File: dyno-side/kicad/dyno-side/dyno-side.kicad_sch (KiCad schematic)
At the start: 18 parts, among them J1 01x02, J2 01x02, J3 01x02, U1 AP2205-50W5-7, U2 TLV9001IDCK, U3 AM26LS32ACN

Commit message: schematics finished -> Waiting for Altium membership to be progressed.
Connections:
- net +5V: now also U3.15 (4B), U3.7 (2B), U3.9 (3B)
- net GND: now also U3.10 (3A), U3.14 (4A), U3.6 (2A)
- no-connect marks 10 -> 4
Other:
- moved on the sheet: C2
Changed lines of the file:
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@@
 	)
 	(junction
+		(at 104.14 50.8)
+		(diameter 0)
+		(color 0 0 0 0)
+	)
+	(junction
+		(at 184.15 38.1)
+		(diameter 0)
+		(color 0 0 0 0)
+	)
+	(junction
 		(at 34.29 43.18)
 		(diameter 0)
@@
 	)
 	(junction
+		(at 107.95 53.34)
+		(diameter 0)
+		(color 0 0 0 0)
+	)
+	(junction
+		(at 104.14 60.96)
+		(diameter 0)
+		(color 0 0 0 0)
+	)
+	(junction
+		(at 104.14 55.88)
+		(diameter 0)
+		(color 0 0 0 0)
+	)
+	(junction
 		(at 173.99 38.1)
 		(diameter 0)
@@
 	)
 	(junction
-		(at 185.42 38.1)
+		(at 107.95 48.26)
+		(diameter 0)
+		(color 0 0 0 0)
+	)
+	(junction
+		(at 107.95 58.42)
 		(diameter 0)
 		(color 0 0 0 0)
@@
 	)
 	(no_connect
-		(at 111.76 50.8)
-	)
-	(no_connect
-		(at 111.76 55.88)
-	)
-	(no_connect
 		(at 147.32 40.64)
 	)
 	(no_connect
-		(at 111.76 43.18)
-	)
-	(no_connect
-		(at 111.76 48.26)
-	)
-	(no_connect
-		(at 111.76 45.72)
-	)
-	(no_connect
 		(at 147.32 43.18)
 	)
@@
 		(at 264.16 43.18)
 	)
-	(no_connect
-		(at 111.76 53.34)
-	)
 	(wire
 		(pts
@@
 	(wire
 		(pts
-			(xy 185.42 38.1) (xy 204.47 38.1)
-		)
-		(stroke
-			(width 0)
-			(type default)
-		)
-	)
-	(wire
-		(pts
 			(xy 60.96 34.29) (xy 63.5 34.29)
 		)
@@
 	(wire
 		(pts
-			(xy 96.52 60.96) (xy 111.76 60.96)
+			(xy 96.52 60.96) (xy 104.14 60.96)
 		)
 		(stroke
@@
 	(wire
 		(pts
+			(xy 107.95 43.18) (xy 107.95 48.26)
+		)
+		(stroke
+			(width 0)
+			(type default)
+		)
+	)
+	(wire
+		(pts
 			(xy 30.48 45.72) (xy 29.21 45.72)
 		)
@@
 	(wire
 		(pts
+			(xy 111.76 43.18) (xy 107.95 43.18)
+		)
+		(stroke
+			(width 0)
+			(type default)
+		)
+	)
+	(wire
+		(pts
+			(xy 107.95 48.26) (xy 107.95 53.34)
+		)
+		(stroke
+			(width 0)
+			(type default)
+		)
+	)
+	(wire
+		(pts
+			(xy 104.14 60.96) (xy 111.76 60.96)
+		)
+		(stroke
+			(width 0)
+			(type default)
+		)
+	)
+	(wire
+		(pts
 			(xy 39.37 27.94) (xy 55.88 27.94)
 		)
@@
 		)
 	)
+	(wire
+		(pts
+			(xy 107.95 53.34) (xy 107.95 58.42)
+		)
+		(stroke
+			(width 0)
+			(type default)
+		)
+	)
 	(polyline
 		(pts
@@
 	(wire
 		(pts
+			(xy 104.14 50.8) (xy 104.14 55.88)
+		)
+		(stroke
+			(width 0)
+			(type default)
+		)
+	)
+	(wire
+		(pts
+			(xy 111.76 48.26) (xy 107.95 48.26)
+		)
+		(stroke
+			(width 0)
+			(type default)
+		)
+	)
+	(wire
+		(pts
 			(xy 83.82 26.67) (xy 83.82 34.29)
 		)
@@
 	(wire
 		(pts
-			(xy 185.42 54.61) (xy 185.42 49.53)
+			(xy 184.15 49.53) (xy 184.15 54.61)
 		)
 		(stroke
@@
 	(wire
 		(pts
-			(xy 182.88 38.1) (xy 185.42 38.1)
+			(xy 104.14 45.72) (xy 104.14 50.8)
+		)
+		(stroke
+			(width 0)
+			(type default)
+		)
+	)
+	(wire
+		(pts
+			(xy 182.88 38.1) (xy 184.15 38.1)
+		)
+		(stroke
+			(width 0)
+			(type default)
+		)
+	)
+	(wire
+		(pts
+			(xy 111.76 50.8) (xy 104.14 50.8)
 		)
 		(stroke
@@
 	(wire
 		(pts
-			(xy 185.42 38.1) (xy 185.42 44.45)
+			(xy 184.15 38.1) (xy 184.15 44.45)
 		)
 		(stroke
@@
 	(wire
 		(pts
+			(xy 111.76 55.88) (xy 104.14 55.88)
+		)
+		(stroke
+			(width 0)
+			(type default)
+		)
+	)
+	(wire
+		(pts
 			(xy 209.55 48.26) (xy 209.55 54.61)
 		)
@@
 	(wire
 		(pts
+			(xy 111.76 53.34) (xy 107.95 53.34)
+		)
+		(stroke
+			(width 0)
+			(type default)
+		)
+	)
+	(wire
+		(pts
 			(xy 55.88 34.29) (xy 55.88 38.1)
 		)
@@
 		)
 	)
+	(wire
+		(pts
+			(xy 184.15 38.1) (xy 204.47 38.1)
+		)
+		(stroke
+			(width 0)
+			(type default)
+		)
+	)
 	(polyline
 		(pts
@@
 	(wire
 		(pts
-			(xy 111.76 58.42) (xy 109.22 58.42)
+			(xy 111.76 58.42) (xy 107.95 58.42)
+		)
+		(stroke
+			(width 0)
+			(type default)
+		)
+	)
+	(wire
+		(pts
+			(xy 104.14 55.88) (xy 104.14 60.96)
+		)
+		(stroke
+			(width 0)
+			(type default)
+		)
+	)
+	(wire
+		(pts
+			(xy 111.76 45.72) (xy 104.14 45.72)
 		)
 		(stroke
@@
 	(wire
 		(pts
-			(xy 109.22 58.42) (xy 109.22 69.85)
+			(xy 107.95 58.42) (xy 107.95 69.85)
 		)
 		(stroke
@@
 	)
 	(global_label "+Signal"
-		(shape output)
+		(shape input)
 		(at 109.22 38.1 180)
 		(fields_autoplaced yes)
@@
 	)
 	(global_label "-Signal"
-		(shape output)
+		(shape input)
 		(at 109.22 40.64 180)
 		(fields_autoplaced yes)
@@
 	(symbol
 		(lib_id "power:GND")
-		(at 185.42 54.61 0)
+		(at 184.15 54.61 0)
 		(unit 1)
 		(body_style 1)
@@
 		(dnp no)
 		(property "Reference" "#PWR04"
-			(at 185.42 60.96 0)
+			(at 184.15 60.96 0)
 			(hide yes)
 			(show_name no)
@@
 		)
 		(property "Value" "GND"
-			(at 185.42 58.674 0)
+			(at 184.15 58.674 0)
 			(show_name no)
 			(do_not_autoplace no)
@@
 		)
 		(property "Footprint" ""
-			(at 185.42 54.61 0)
+			(at 184.15 54.61 0)
 			(hide yes)
 			(show_name no)
@@
 		)
 		(property "Datasheet" ""
-			(at 185.42 54.61 0)
+			(at 184.15 54.61 0)
 			(hide yes)
 			(show_name no)
@@
 		)
 		(property "Description" "Power symbol creates a global label with name \"GND\" , ground"
-			(at 185.42 54.61 0)
+			(at 184.15 54.61 0)
 			(hide yes)
 			(show_name no)
@@
 	(symbol
 		(lib_id "power:GND")
-		(at 109.22 69.85 0)
+		(at 107.95 69.85 0)
 		(unit 1)
 		(body_style 1)
@@
 		(dnp no)
 		(property "Reference" "#PWR016"
-			(at 109.22 76.2 0)
+			(at 107.95 76.2 0)
 			(hide yes)
 			(show_name no)
@@
 		)
 		(property "Value" "GND"
-			(at 109.22 73.914 0)
+			(at 107.95 73.914 0)
 			(show_name no)
 			(do_not_autoplace no)
@@
 		)
 		(property "Footprint" ""
-			(at 109.22 69.85 0)
+			(at 107.95 69.85 0)
 			(hide yes)
 			(show_name no)
@@
 		)
 		(property "Datasheet" ""
-			(at 109.22 69.85 0)
+			(at 107.95 69.85 0)
 			(hide yes)
 			(show_name no)
@@
 		)
 		(property "Description" "Power symbol creates a global label with name \"GND\" , ground"
-			(at 109.22 69.85 0)
+			(at 107.95 69.85 0)
 			(hide yes)
 			(show_name no)
@@
 	(symbol
 		(lib_id "Device:C_Small")
-		(at 185.42 46.99 0)
+		(at 184.15 46.99 0)
 		(unit 1)
 		(body_style 1)
@@
 		(fields_autoplaced yes)
 		(property "Reference" "C2"
-			(at 187.96 45.7262 0)
+			(at 186.69 45.7262 0)
 			(show_name no)
 			(do_not_autoplace no)
@@
 		)
 		(property "Value" "1.5uF"
-			(at 187.96 48.2662 0)
+			(at 186.69 48.2662 0)
 			(show_name no)
 			(do_not_autoplace no)
@@
 		)
 		(property "Footprint" ""
-			(at 185.42 46.99 0)
+			(at 184.15 46.99 0)
 			(hide yes)
 			(show_name no)
@@
 		)
 		(property "Datasheet" ""
-			(at 185.42 46.99 0)
+			(at 184.15 46.99 0)
 			(hide yes)
 			(show_name no)
@@
 		)
 		(property "Description" "Unpolarized capacitor, small symbol"
-			(at 185.42 46.99 0)
+			(at 184.15 46.99 0)
 			(hide yes)
 			(show_name no)

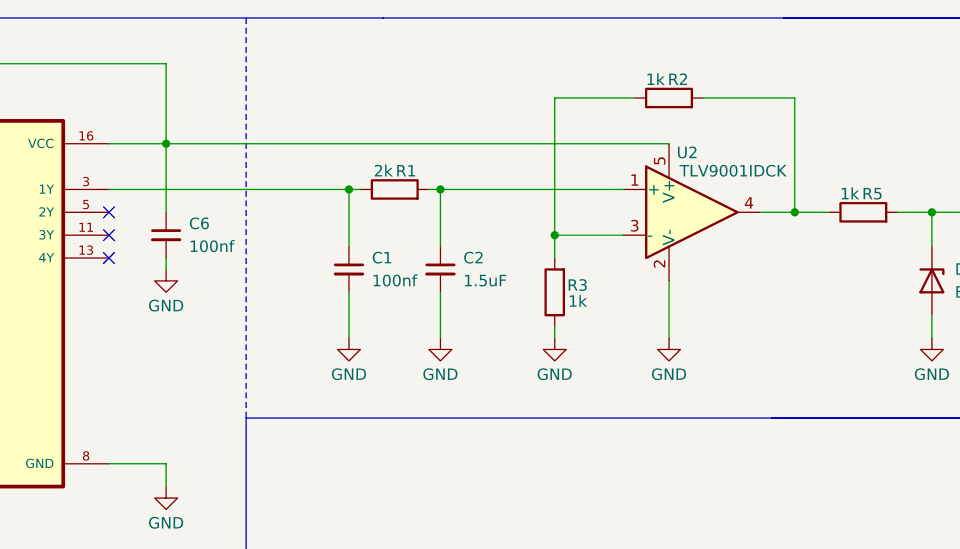
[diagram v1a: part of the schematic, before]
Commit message: corrections tlv9002 replaced with lm458 & ecu 5v domain not 3.3v domain.
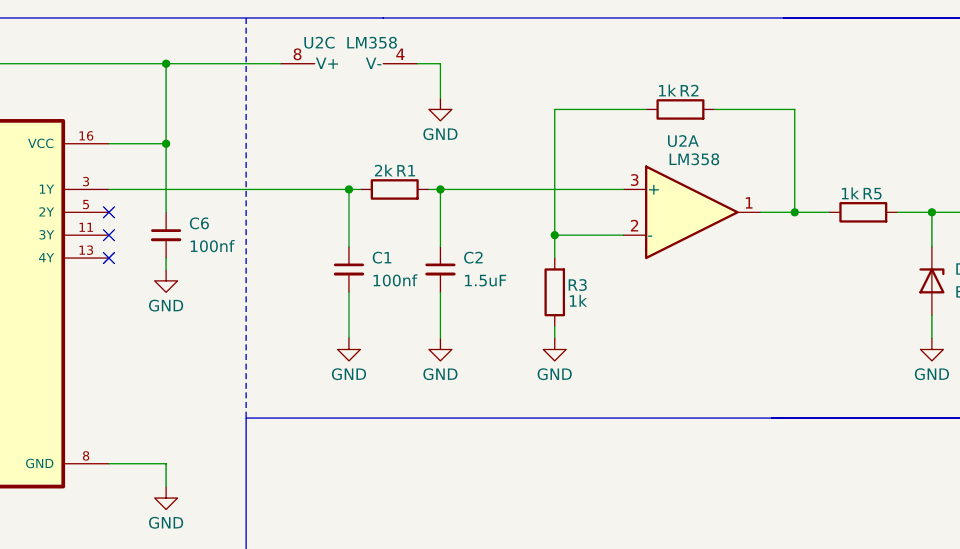
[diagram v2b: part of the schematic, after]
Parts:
- removed U2: TLV9001IDCK, Package_TO_SOT_SMD:SOT-353_SC-70-5, symbol Amplifier_Operational:TLV9001IDCK
- added U2: LM358, symbol Amplifier_Operational:LM358
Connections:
- net +5V: now also U2.8 (V+)
- net GND: now also U2.4 (V-)
- net at R2.2, R5.1: now also U2.1
- net at R2.1, R3.2: now also U2.2 (-)
- net at C2.1, R1.2: now also U2.3 (+)
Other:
- moved on the sheet: R2

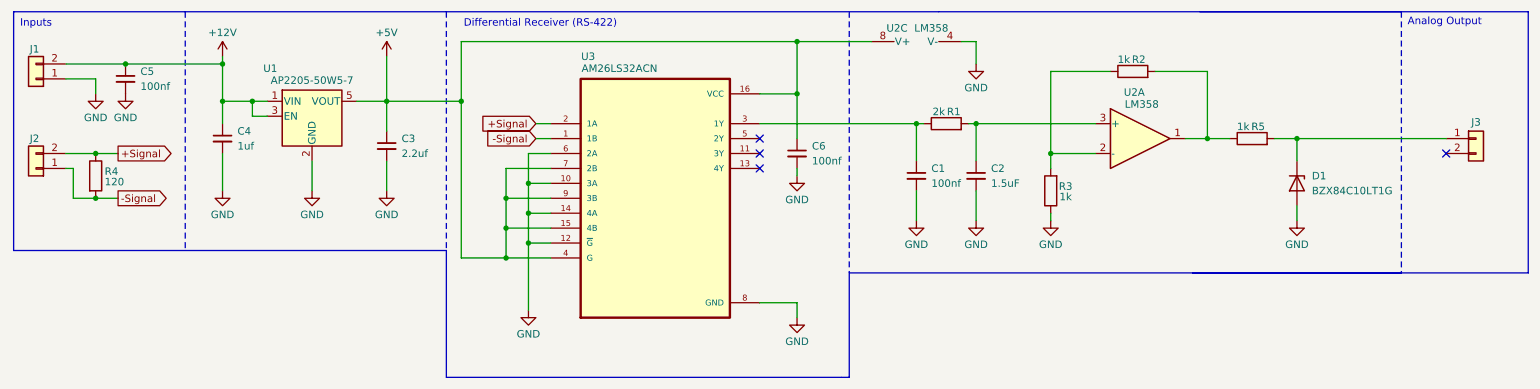
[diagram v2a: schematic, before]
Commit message: Fixed op-amp mistake (wrong source) & deceased op-amp output impedance.
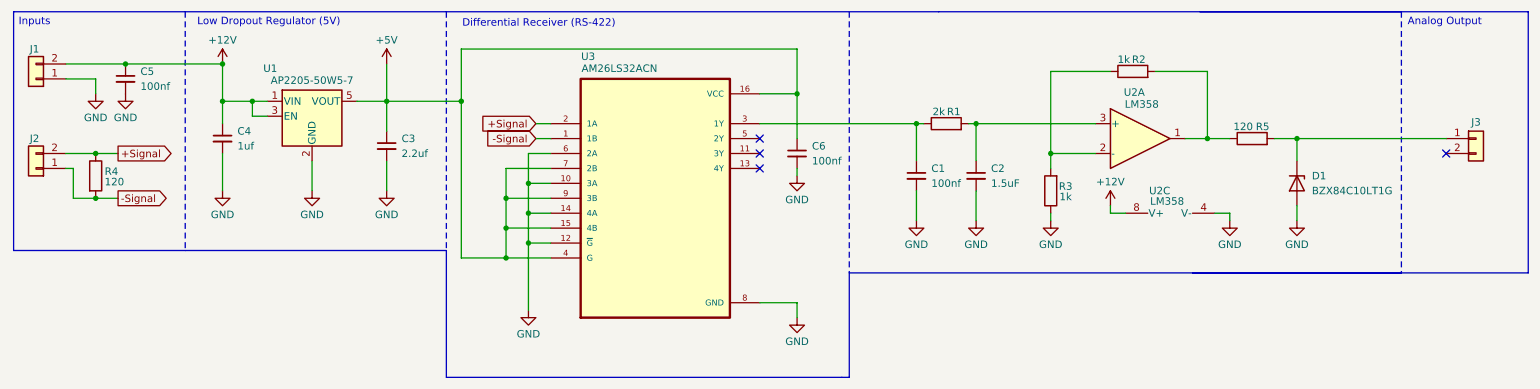
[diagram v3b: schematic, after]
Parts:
- R5: value 1k -> 120
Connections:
- net +12V: now also U2.8 (V+)
- net +5V: no longer U2.8 (V+)
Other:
- note added: "Low Dropout Regulator (5V)"
- moved on the sheet: U2C
